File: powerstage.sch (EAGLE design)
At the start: 38 parts, among them CON1 PINHEAD_1X10-2-FEMALE, CON2 BATTERY_CON-2P-XT30-RA, CON3 PINHEAD_1X10-2-FEMALE, IC5 MCP9700, Q1 BUK7K6R2-40EX, Q2 BUK7K6R2-40EX, Q3 BUK7K6R2-40EX

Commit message: powerstage updates
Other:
- note added: "1727-7274-1-ND MOSFET 2N-CH 40V 40A LFPAK56D 1727-2462-1-ND MOSFET 2N-CH 60V 40A LFPAK56"
- note added: "732-8860-1-ND 68uF 50V capacitor"
- note added: "the only difference between 8S and 10S versions is MOSFET and capacitor selection"
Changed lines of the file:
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@@
 as close to negative supply pad as possible</text>
 <text x="142.24" y="149.86" size="2.54" layer="97">Place close to power mosfets</text>
+<text x="38.1" y="25.4" size="1.778" layer="91">1727-7274-1-ND  MOSFET 2N-CH 40V 40A LFPAK56D
+1727-2462-1-ND  MOSFET 2N-CH 60V 40A LFPAK56</text>
+<text x="35.56" y="45.72" size="1.778" layer="91">the only difference between
+8S and 10S versions is MOSFET
+and capacitor selection</text>
+<text x="38.1" y="15.24" size="1.778" layer="91">732-8860-1-ND 68uF 50V capacitor</text>
 </plain>
 <instances>

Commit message: DUCK is here
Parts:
- C1, C2, C3, C4: value (none) -> 68µF; device rc:CPOLRADIAL-6.3X12.5-RA -> rc:CPOL-68UF_50VRADIAL-6.3X12.5-RA
- C31, C35, C58, C62, C63, C64: value 4.7µF -> 10µF; device myxa_masterlib:4.7µF-100V_20%_X7S-1210 -> C_digikey:10µF-50V_20%_X5R-C1210
- C5, C6: value (none) -> 68µF; DIGIKEY# (none) -> 732-8860-1-ND; PACKAGE (none) -> RADIAL
- Q1, Q2, Q3: value BUK7K6R2-40EX -> BUK9K6R2-40E,115; device mosfet:BUK7K6R2-40EX -> mosfet:BUK9K6R2-40E,115
- R18, R5: value 1 mOhms -> 3 mOhms; device SHUNT_RESISTORS:CURRENT_SHUNT_KELVIN-0.001R-2512-KELVIN -> SHUNT_RESISTORS:CURRENT_SHUNT_KELVIN-0.003R-2512-KELVIN
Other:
- moved on the sheet: D4

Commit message: poly update
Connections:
- net PGND: now also CON2.PAD1, CON2.PAD2
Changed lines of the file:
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@@
 <pinref part="D4" gate="G$1" pin="A"/>
 <wire x1="116.84" y1="220.98" x2="116.84" y2="223.52" width="0.1524" layer="91"/>
+<pinref part="CON2" gate="G$1" pin="PAD1"/>
+<wire x1="35.56" y1="223.52" x2="35.56" y2="220.98" width="0.1524" layer="91"/>
+<wire x1="35.56" y1="220.98" x2="45.72" y2="220.98" width="0.1524" layer="91"/>
+<junction x="45.72" y="220.98"/>
+<pinref part="CON2" gate="G$1" pin="PAD2"/>
+<wire x1="35.56" y1="231.14" x2="35.56" y2="233.68" width="0.1524" layer="91"/>
+<wire x1="35.56" y1="233.68" x2="30.48" y2="233.68" width="0.1524" layer="91"/>
+<wire x1="30.48" y1="233.68" x2="30.48" y2="220.98" width="0.1524" layer="91"/>
+<wire x1="30.48" y1="220.98" x2="35.56" y2="220.98" width="0.1524" layer="91"/>
+<junction x="35.56" y="220.98"/>
 </segment>
 <segment>

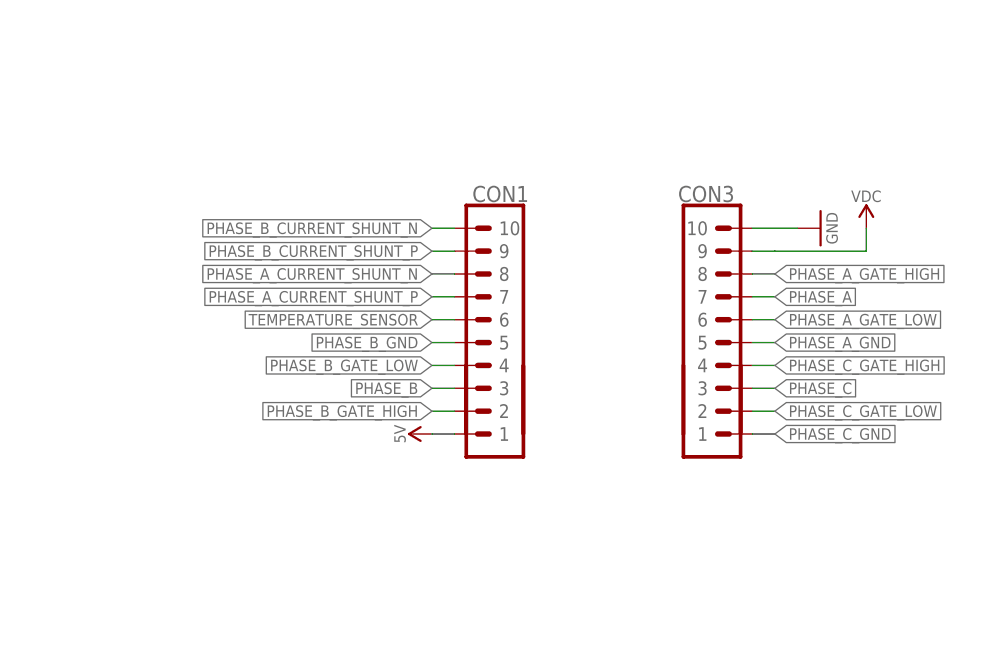
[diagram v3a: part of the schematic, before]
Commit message: pinout fixes
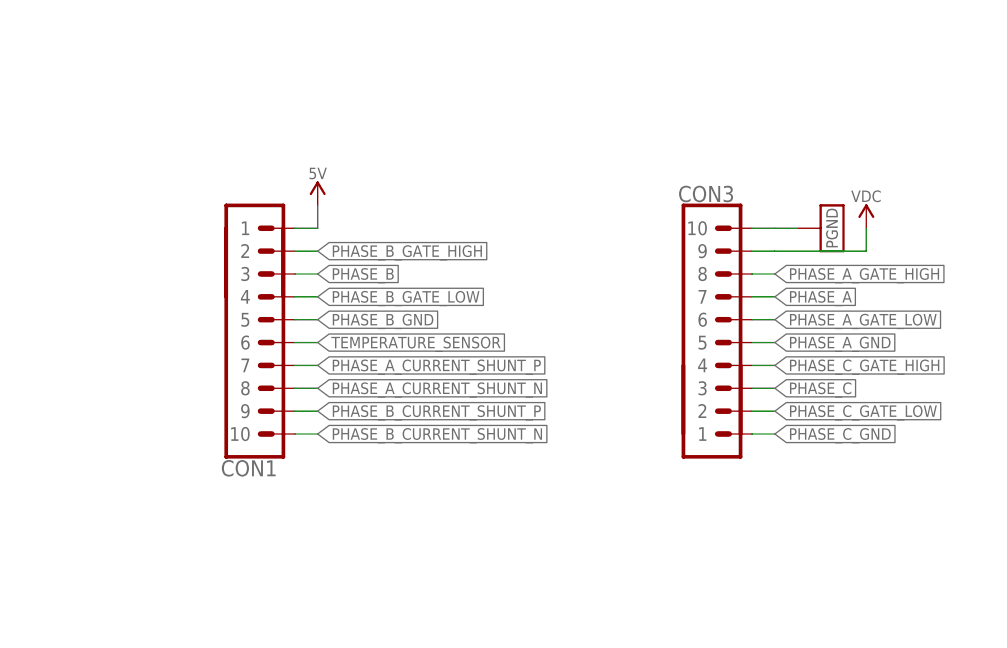
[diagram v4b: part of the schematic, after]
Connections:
- removed net GND: CON3.10
- net PGND: now also CON3.10
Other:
- moved on the sheet: CON1
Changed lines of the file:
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@@
 <part name="D2" library="TVS_diodes" library_urn="urn:adsk.eagle:library:3333632" deviceset="PTVS36VP1UP,115" device="-SOD128" package3d_urn="urn:adsk.eagle:package:6533206/2" technology="-36V"/>
 <part name="+P1" library="supply_symbols" library_urn="urn:adsk.eagle:library:5017758" deviceset="5V" device=""/>
-<part name="GND1" library="supply_symbols" library_urn="urn:adsk.eagle:library:5017758" deviceset="GND" device="" value="GND"/>
 <part name="+P2" library="supply_symbols" library_urn="urn:adsk.eagle:library:5017758" deviceset="VDC" device=""/>
 <part name="GND5" library="supply_symbols" library_urn="urn:adsk.eagle:library:5017758" deviceset="PGND" device="" value="PGND"/>
 <part name="D3" library="TVS_diodes" library_urn="urn:adsk.eagle:library:3333632" deviceset="PTVS36VP1UP,115" device="-SOD128" package3d_urn="urn:adsk.eagle:package:6533206/2" technology="-36V"/>
 <part name="D4" library="TVS_diodes" library_urn="urn:adsk.eagle:library:3333632" deviceset="PTVS36VP1UP,115" device="-SOD128" package3d_urn="urn:adsk.eagle:package:6533206/2" technology="-36V"/>
+<part name="GND7" library="supply_symbols" library_urn="urn:adsk.eagle:library:5017758" deviceset="PGND" device="" value="PGND"/>
 </parts>
 <sheets>
@@
 <attribute name="PACKAGE" x="358.14" y="198.882" size="0.762" layer="96" font="vector" ratio="15" align="center-right"/>
 </instance>
-<instance part="CON1" gate="G$1" x="175.26" y="96.52" smashed="yes" rot="MR0">
-<attribute name="NAME" x="172.72" y="125.73" size="1.778" layer="95" font="vector" ratio="15" rot="MR0" align="center"/>
+<instance part="CON1" gate="G$1" x="142.24" y="124.46" smashed="yes" rot="MR180">
+<attribute name="NAME" x="144.78" y="95.25" size="1.778" layer="95" font="vector" ratio="15" rot="MR180" align="center"/>
 </instance>
 <instance part="CON3" gate="G$1" x="193.04" y="96.52" smashed="yes">
@@
 <attribute name="MANF#" x="73.66" y="228.6" size="1.016" layer="95" font="vector" ratio="15" rot="R90" align="center"/>
 </instance>
-<instance part="+P1" gate="G$1" x="165.1" y="99.06" smashed="yes" rot="R90">
-<attribute name="VALUE" x="161.544" y="99.06" size="1.27" layer="96" font="vector" ratio="15" rot="R90" align="center"/>
-</instance>
-<instance part="GND1" gate="1" x="208.28" y="121.92" smashed="yes" rot="MR270">
-<attribute name="VALUE" x="209.55" y="121.92" size="1.27" layer="96" font="vector" ratio="15" rot="MR270" align="center"/>
+<instance part="+P1" gate="G$1" x="152.4" y="124.46" smashed="yes">
+<attribute name="VALUE" x="152.4" y="128.016" size="1.27" layer="96" font="vector" ratio="15" align="center"/>
 </instance>
 <instance part="+P2" gate="G$1" x="213.36" y="121.92" smashed="yes">
@@
 <attribute name="NAME" x="114.3" y="226.06" size="1.27" layer="95" font="vector" ratio="15" rot="R90" align="center"/>
 <attribute name="MANF#" x="119.38" y="226.06" size="1.016" layer="95" font="vector" ratio="15" rot="R90" align="center"/>
+</instance>
+<instance part="GND7" gate="G$1" x="208.28" y="121.92" smashed="yes" rot="R90">
+<attribute name="VALUE" x="209.55" y="121.92" size="1.27" layer="97" font="vector" ratio="15" rot="R90" align="center"/>
 </instance>
 </instances>
@@
 </busses>
 <nets>
-<net name="GND" class="0">
-<segment>
-<pinref part="CON3" gate="G$1" pin="10"/>
-<wire x1="200.66" y1="121.92" x2="203.2" y2="121.92" width="0.1524" layer="91"/>
-<pinref part="GND1" gate="1" pin="GND"/>
-<wire x1="203.2" y1="121.92" x2="205.74" y2="121.92" width="0.1524" layer="91"/>
-</segment>
-</net>
 <net name="PHASE_A_GND" class="0">
 <segment>
@@
 <segment>
 <pinref part="CON1" gate="G$1" pin="8"/>
-<wire x1="167.64" y1="116.84" x2="165.1" y2="116.84" width="0.1524" layer="91"/>
-<label x="165.1" y="116.84" size="1.27" layer="95" rot="MR0" xref="yes"/>
+<wire x1="149.86" y1="104.14" x2="152.4" y2="104.14" width="0.1524" layer="91"/>
+<label x="152.4" y="104.14" size="1.27" layer="95" rot="MR180" xref="yes"/>
 </segment>
 </net>
@@
 <segment>
 <pinref part="CON1" gate="G$1" pin="7"/>
-<wire x1="167.64" y1="114.3" x2="165.1" y2="114.3" width="0.1524" layer="91"/>
-<label x="165.1" y="114.3" size="1.27" layer="95" rot="MR0" xref="yes"/>
+<wire x1="149.86" y1="106.68" x2="152.4" y2="106.68" width="0.1524" layer="91"/>
+<label x="152.4" y="106.68" size="1.27" layer="95" rot="MR180" xref="yes"/>
 </segment>
 </net>
@@
 <segment>
 <pinref part="CON1" gate="G$1" pin="2"/>
-<wire x1="167.64" y1="101.6" x2="165.1" y2="101.6" width="0.1524" layer="91"/>
-<label x="165.1" y="101.6" size="1.27" layer="95" rot="MR0" xref="yes"/>
+<wire x1="149.86" y1="119.38" x2="152.4" y2="119.38" width="0.1524" layer="91"/>
+<label x="152.4" y="119.38" size="1.27" layer="95" rot="MR180" xref="yes"/>
 </segment>
 <segment>
@@
 <segment>
 <pinref part="CON1" gate="G$1" pin="4"/>
-<wire x1="167.64" y1="106.68" x2="165.1" y2="106.68" width="0.1524" layer="91"/>
-<label x="165.1" y="106.68" size="1.27" layer="95" rot="MR0" xref="yes"/>
+<wire x1="149.86" y1="114.3" x2="152.4" y2="114.3" width="0.1524" layer="91"/>
+<label x="152.4" y="114.3" size="1.27" layer="95" rot="MR180" xref="yes"/>
 </segment>
 <segment>
@@
 <segment>
 <pinref part="CON1" gate="G$1" pin="5"/>
-<wire x1="167.64" y1="109.22" x2="165.1" y2="109.22" width="0.1524" layer="91"/>
-<label x="165.1" y="109.22" size="1.27" layer="95" rot="MR0" xref="yes"/>
+<wire x1="149.86" y1="111.76" x2="152.4" y2="111.76" width="0.1524" layer="91"/>
+<label x="152.4" y="111.76" size="1.27" layer="95" rot="MR180" xref="yes"/>
 </segment>
 <segment>
@@
 <segment>
 <pinref part="CON1" gate="G$1" pin="10"/>
-<wire x1="167.64" y1="121.92" x2="165.1" y2="121.92" width="0.1524" layer="91"/>
-<label x="165.1" y="121.92" size="1.27" layer="95" rot="MR0" xref="yes"/>
+<wire x1="149.86" y1="99.06" x2="152.4" y2="99.06" width="0.1524" layer="91"/>
+<label x="152.4" y="99.06" size="1.27" layer="95" rot="MR180" xref="yes"/>
 </segment>
 </net>
@@
 <segment>
 <pinref part="CON1" gate="G$1" pin="9"/>
-<wire x1="167.64" y1="119.38" x2="165.1" y2="119.38" width="0.1524" layer="91"/>
-<label x="165.1" y="119.38" size="1.27" layer="95" rot="MR0" xref="yes"/>
+<wire x1="149.86" y1="101.6" x2="152.4" y2="101.6" width="0.1524" layer="91"/>
+<label x="152.4" y="101.6" size="1.27" layer="95" rot="MR180" xref="yes"/>
 </segment>
 </net>
@@
 <segment>
 <pinref part="CON1" gate="G$1" pin="3"/>
-<wire x1="167.64" y1="104.14" x2="165.1" y2="104.14" width="0.1524" layer="91"/>
-<label x="165.1" y="104.14" size="1.27" layer="95" rot="MR0" xref="yes"/>
+<wire x1="149.86" y1="116.84" x2="152.4" y2="116.84" width="0.1524" layer="91"/>
+<label x="152.4" y="116.84" size="1.27" layer="95" rot="MR180" xref="yes"/>
 </segment>
 <segment>
@@
 <segment>
 <pinref part="CON1" gate="G$1" pin="1"/>
-<wire x1="167.64" y1="99.06" x2="165.1" y2="99.06" width="0.1524" layer="91"/>
 <pinref part="+P1" gate="G$1" pin="VDD_5V"/>
+<wire x1="149.86" y1="121.92" x2="152.4" y2="121.92" width="0.1524" layer="91"/>
+<wire x1="152.4" y1="121.92" x2="152.4" y2="124.46" width="0.1524" layer="91"/>
 </segment>
 </net>
@@
 <segment>
 <pinref part="CON1" gate="G$1" pin="6"/>
-<wire x1="167.64" y1="111.76" x2="165.1" y2="111.76" width="0.1524" layer="91"/>
-<label x="165.1" y="111.76" size="1.27" layer="95" rot="MR0" xref="yes"/>
+<wire x1="149.86" y1="109.22" x2="152.4" y2="109.22" width="0.1524" layer="91"/>
+<label x="152.4" y="109.22" size="1.27" layer="95" rot="MR180" xref="yes"/>
 </segment>
 </net>
@@
 <wire x1="167.64" y1="162.56" x2="167.64" y2="160.02" width="0.1524" layer="91"/>
 </segment>
-</net>
+<segment>
+<pinref part="CON3" gate="G$1" pin="10"/>
+<wire x1="200.66" y1="121.92" x2="203.2" y2="121.92" width="0.1524" layer="91"/>
+<wire x1="203.2" y1="121.92" x2="205.74" y2="121.92" width="0.1524" layer="91"/>
+<pinref part="GND7" gate="G$1" pin="PGND"/>
+</segment>
+</net>

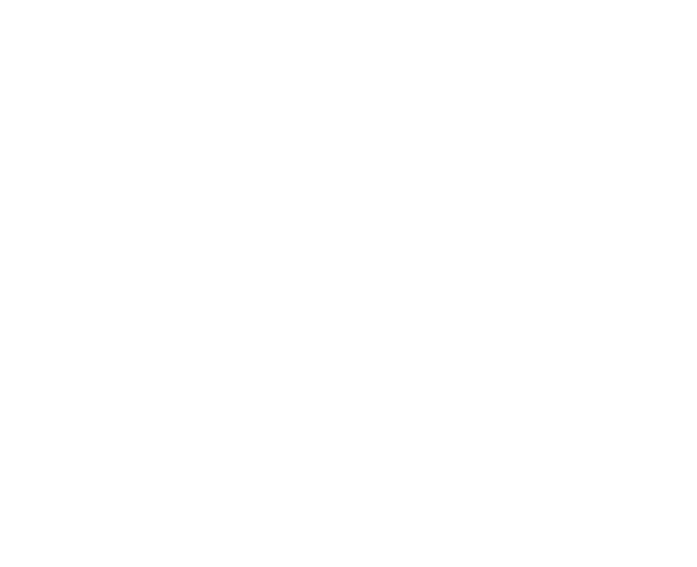
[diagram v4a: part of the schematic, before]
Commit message: fiducial marks
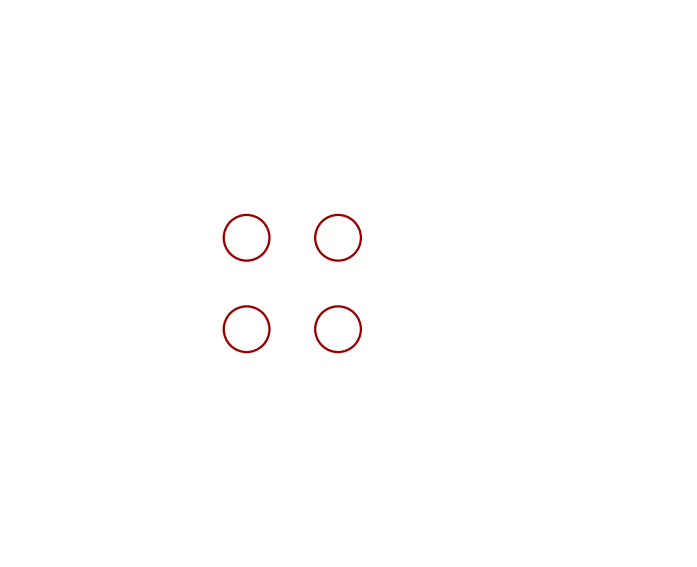
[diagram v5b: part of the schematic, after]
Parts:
- added U$10, U$12, U$8, U$9: FIDUCIALMOUNT, usb2can_master_lib:FIDUCIALMOUNT
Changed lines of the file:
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@@
 </attributes>
 <variantdefs>
-<variantdef name="BASIC"/>
+<variantdef name="BASIC" current="yes"/>
 </variantdefs>
 <classes>
@@
 <part name="D4" library="TVS_diodes" library_urn="urn:adsk.eagle:library:3333632" deviceset="PTVS36VP1UP,115" device="-SOD128" package3d_urn="urn:adsk.eagle:package:6533206/2" technology="-36V"/>
 <part name="GND7" library="supply_symbols" library_urn="urn:adsk.eagle:library:5017758" deviceset="PGND" device="" value="PGND"/>
+<part name="U$8" library="usb2can_master_lib" deviceset="FIDUCIALMOUNT" device="">
+<variant name="BASIC" populate="no"/>
+</part>
+<part name="U$9" library="usb2can_master_lib" deviceset="FIDUCIALMOUNT" device="">
+<variant name="BASIC" populate="no"/>
+</part>
+<part name="U$10" library="usb2can_master_lib" deviceset="FIDUCIALMOUNT" device="">
+<variant name="BASIC" populate="no"/>
+</part>
+<part name="U$12" library="usb2can_master_lib" deviceset="FIDUCIALMOUNT" device="">
+<variant name="BASIC" populate="no"/>
+</part>
 </parts>
 <sheets>
@@
 <attribute name="VALUE" x="209.55" y="121.92" size="1.27" layer="97" font="vector" ratio="15" rot="R90" align="center"/>
 </instance>
+<instance part="U$8" gate="G$1" x="45.72" y="93.98" smashed="yes" rot="R270"/>
+<instance part="U$9" gate="G$1" x="35.56" y="104.14" smashed="yes" rot="R270"/>
+<instance part="U$10" gate="G$1" x="35.56" y="93.98" smashed="yes" rot="R270"/>
+<instance part="U$12" gate="G$1" x="45.72" y="104.14" smashed="yes" rot="R270"/>
 </instances>
 <busses>
